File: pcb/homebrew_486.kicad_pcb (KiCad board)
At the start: 4 copper layers, 150 x 150 mm, 161 parts, among them J1 Bus_ISA_16bit, J11 PEN, J13 KB, J15 PC SPK, J16 ATUART, J18 EXT. RESET, J19 Conn_01x02_Pin, J2 Bus_ISA_16bit, J20 Conn_01x02_Pin, J21 Conn_01x02_Pin, J22 Conn_01x02_Pin, J3 ATX-20, J4 AVR ISP, J5 Cmos settings, J6 Enable load, J9 x2 Multiplier, SW1 SW_SPDT, SW2 Reset, U1 486Socket, U10 8259A-2, U11 HM628512, U12 HM628512, U13 HM628512, U14 HM628512, U15 HM628512, U16 HM628512, U17 HM628512, U18 HM628512, U19 74LS245, U2 XC2S100TQ144, U20 74LS245, U21 W29C020, U22 ATmega128L-8A, U3 AMS1117, U4 AMS1117, U5 74LS245, U6 74LS245, U7 74LS245, U8 74LS245, U9 8254, Y1 TXC-7C, Y2 GTXO-14T, Y3 16MHz

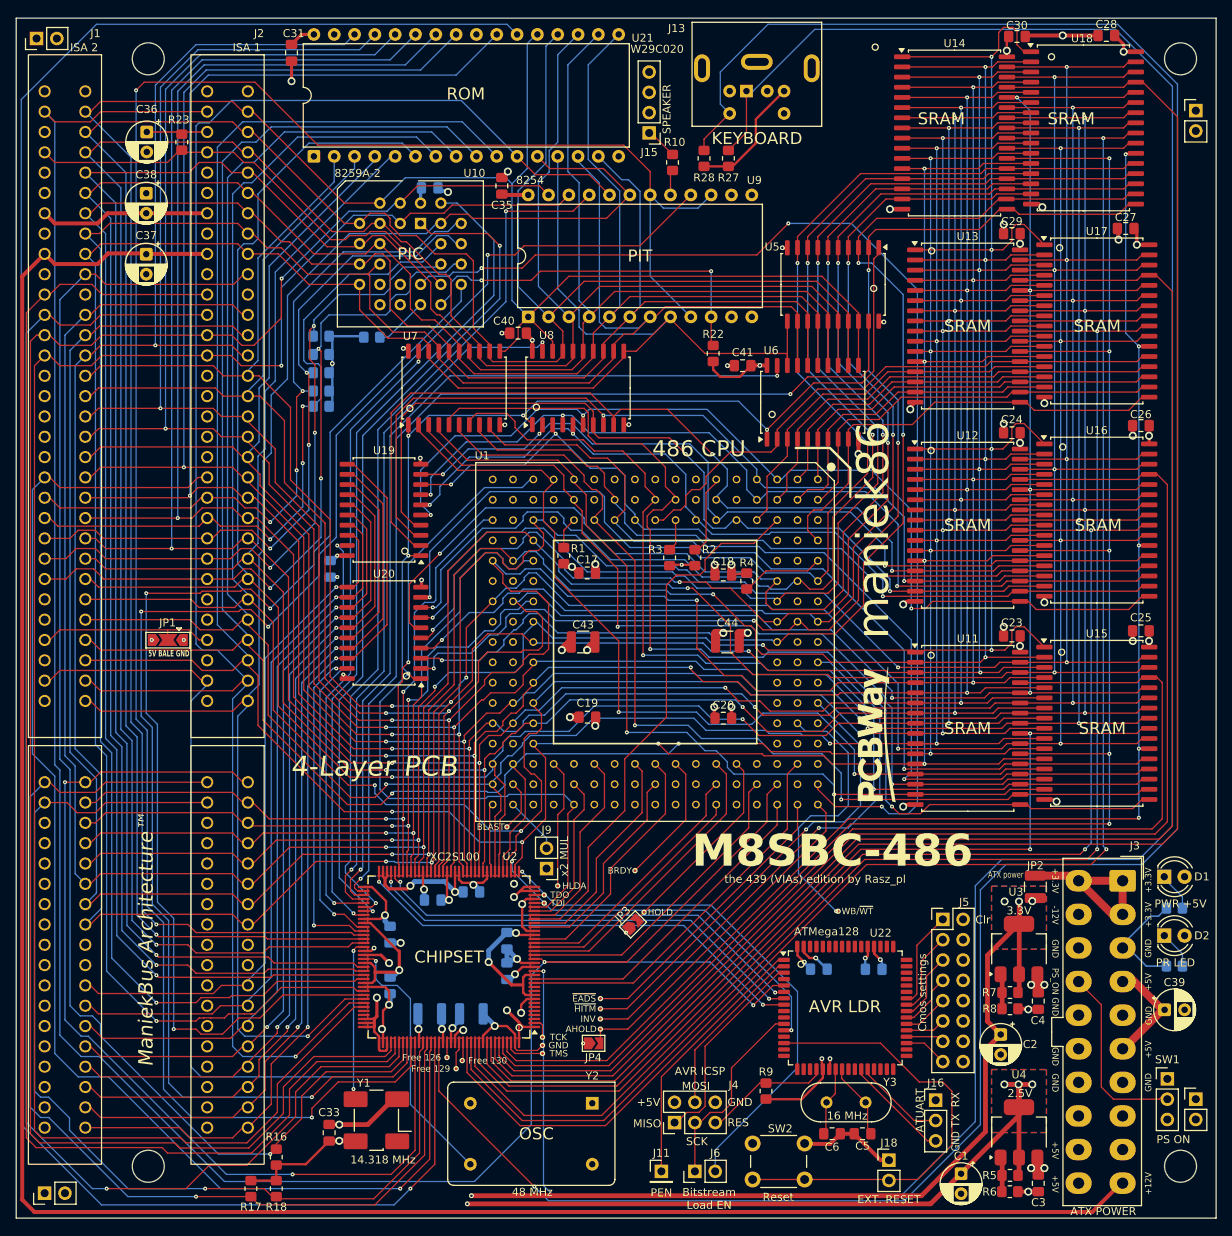
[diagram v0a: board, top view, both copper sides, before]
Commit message: cant use I/GCK for generic input after all, moving ps2_data to another IO. CLKDV_DIVIDE => 12.0 uses two DLLs and blocks CLK_IN_14_318 from using GCK0 -> moving CLK_FPGA to GCK3 instead.
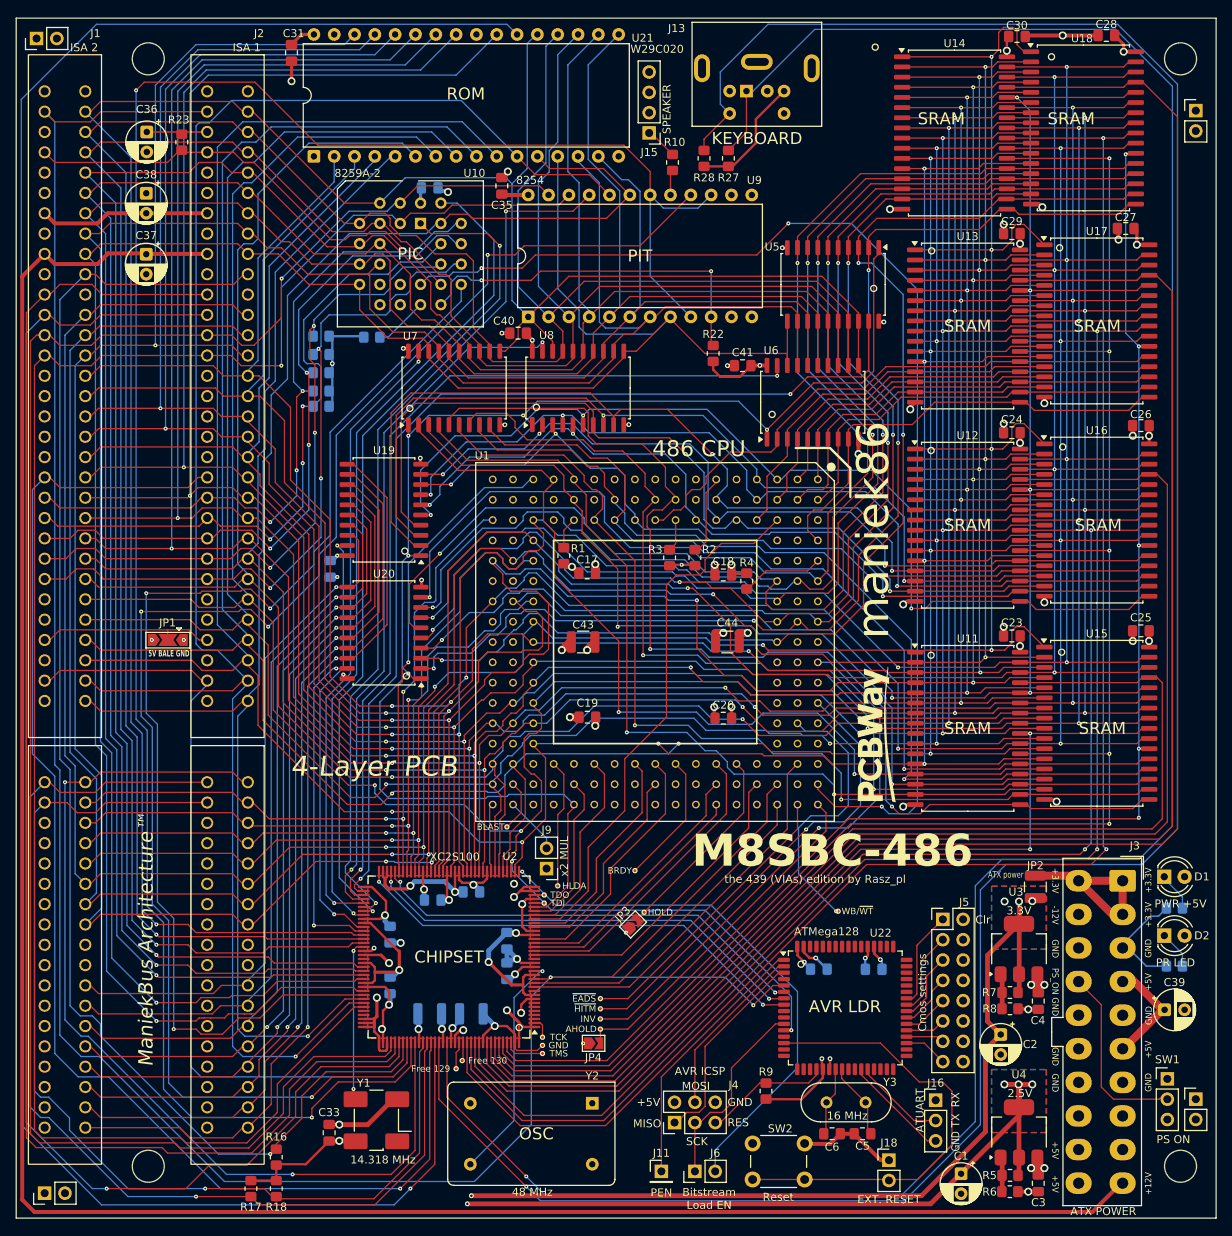
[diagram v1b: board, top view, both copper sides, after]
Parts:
- removed TP15: Free 126, 486custom:TestPoint_Pad_D0.4mm
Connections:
- U2 pad 11: unconnected-(U2-IO-Pad11) -> /CPU/NMI
- U2 pad 12: /CPU/NMI -> /CPU/~{BS16}
- U2 pad 126: Net-(TP15-Pad1) -> /FPGA/PS2_DATA
- U2 pad 13: /CPU/~{BS16} -> /CPU_RESET
- U2 pad 15: /FPGA/PS2_DATA -> /FPGA/CLK_FPGA
- U2 pad 18: /CPU_RESET -> unconnected-(U2-I/GCK2-Pad18)
- U2 pad 91: /FPGA/CLK_FPGA -> unconnected-(U2-I/GCK1-Pad91)
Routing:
- net /FPGA/PS2_DATA: track 303.5 -> 299.1 mm
- net /FPGA/CLK_FPGA: track 33.0 -> 29.0 mm
- net /CPU_RESET: track 303.0 -> 300.6 mm
- net Net-(TP15-Pad1): track 1.91 -> 0.00 mm
- net /FPGA/PS2_CLK: track 308.0 -> 308.6 mm

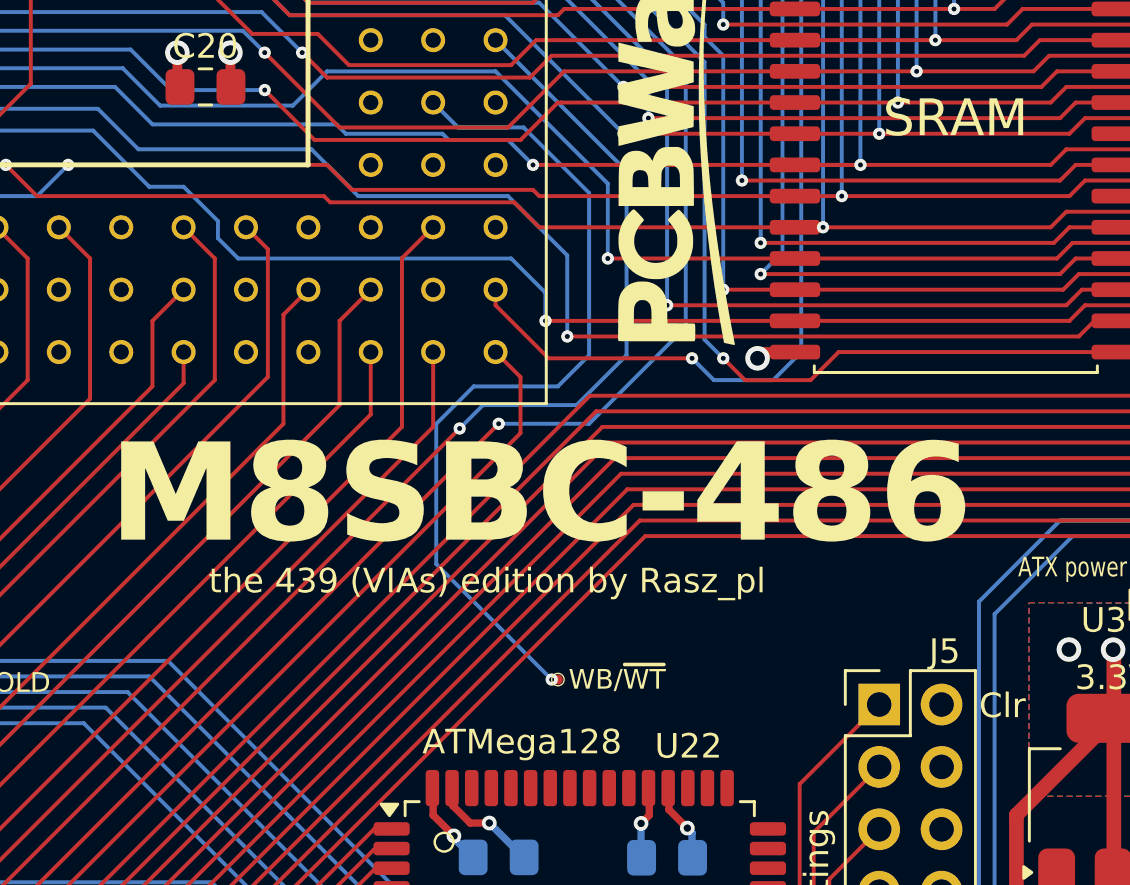
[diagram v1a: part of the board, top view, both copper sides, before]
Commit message: CPU pulled A20M nar the AVR and made pullup optional. Enables control of A20M by AVR like old school Keyboard controllers did in 286.
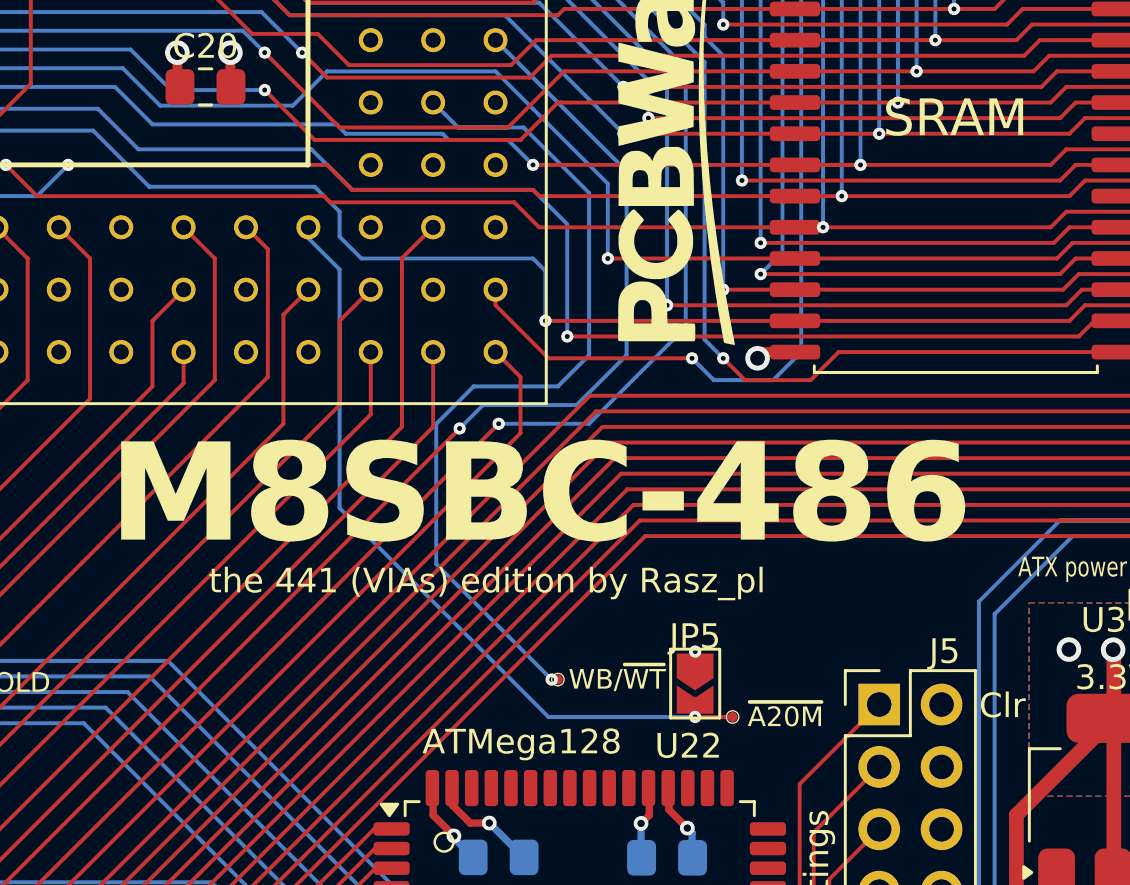
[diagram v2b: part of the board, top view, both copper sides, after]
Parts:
- added JP5: Jumper_2_Open, Jumper:SolderJumper-2_P1.3mm_Open_TrianglePad1.0x1.5mm, F.Cu at (129.9, 134.7)
- added TP15: ~{A20M}, 486custom:TestPoint_Pad_D0.4mm, F.Cu at (131.4, 136.0)
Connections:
- U1 pad D15: +5V -> Net-(JP5-B)
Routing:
- net Net-(JP5-B): track 0.00 -> 32.1 mm, vias 0 -> 1
- net /D4: track 120.4 -> 121.2 mm
- net /D2: track 109.9 -> 110.6 mm
- net +5V: vias 31 -> 32
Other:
- board text added: "the 441 (VIAs) edition by Rasz_pl"
- board text removed: "the 439 (VIAs) edition by Rasz_pl"
